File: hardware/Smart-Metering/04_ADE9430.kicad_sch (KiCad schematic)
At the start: 14 parts, among them U1 ADE9430ACPZ, Y1 24.576MHz

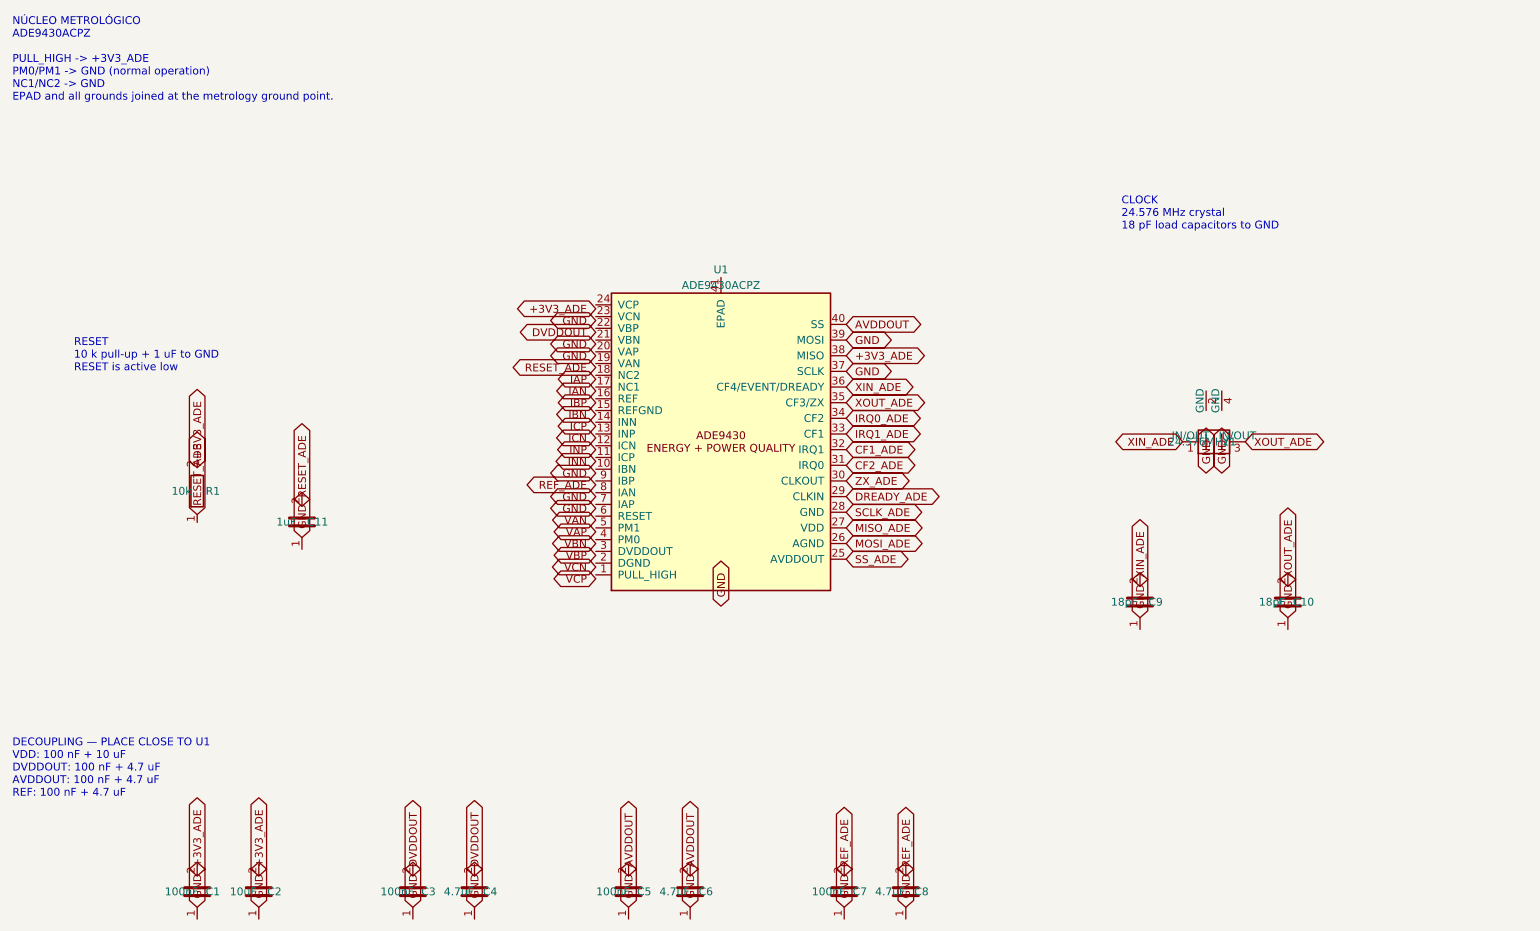
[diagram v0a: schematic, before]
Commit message: Corrige eixo Y dos símbolos próprios e ligações do ADE9430
Os símbolos de SmartMetering.kicad_sym foram escritos com o eixo Y
para baixo, mas o formato de biblioteca do KiCad usa Y para cima.
Com isso, na folha 04_ADE9430:

- os pinos 1-24 e o EPAD do U1 ficavam desconectados;
- os pinos 25-40 caíam em labels trocados (AVDDOUT em SS_ADE,
  VDD em MISO_ADE, SCLK/MOSI em GND etc.);
- os pinos GND do cristal Y1 ficavam desconectados;
- as pernas dos pinos verticais (R, C, cristal, EPAD) apontavam
  para fora do corpo do símbolo.

Correção: inverter o Y de pinos, propriedades e gráficos e orientar
os pinos verticais para o corpo, na biblioteca e na cópia embutida
na folha. Agora o pino 1 do ADE9430 fica no canto superior esquerdo
e todos os 69 pinos da folha caem nos nets previstos. O label GND
do EPAD passa a apontar para baixo.

Atualiza também a estrutura e o estado do projeto no README.

Co-Authored-By: Claude Opus 5.5 <noreply@anthropic.com>
Claude-Session: https://claude.ai/code/session_012B8cVkhtjf3eg98UdpNCpf
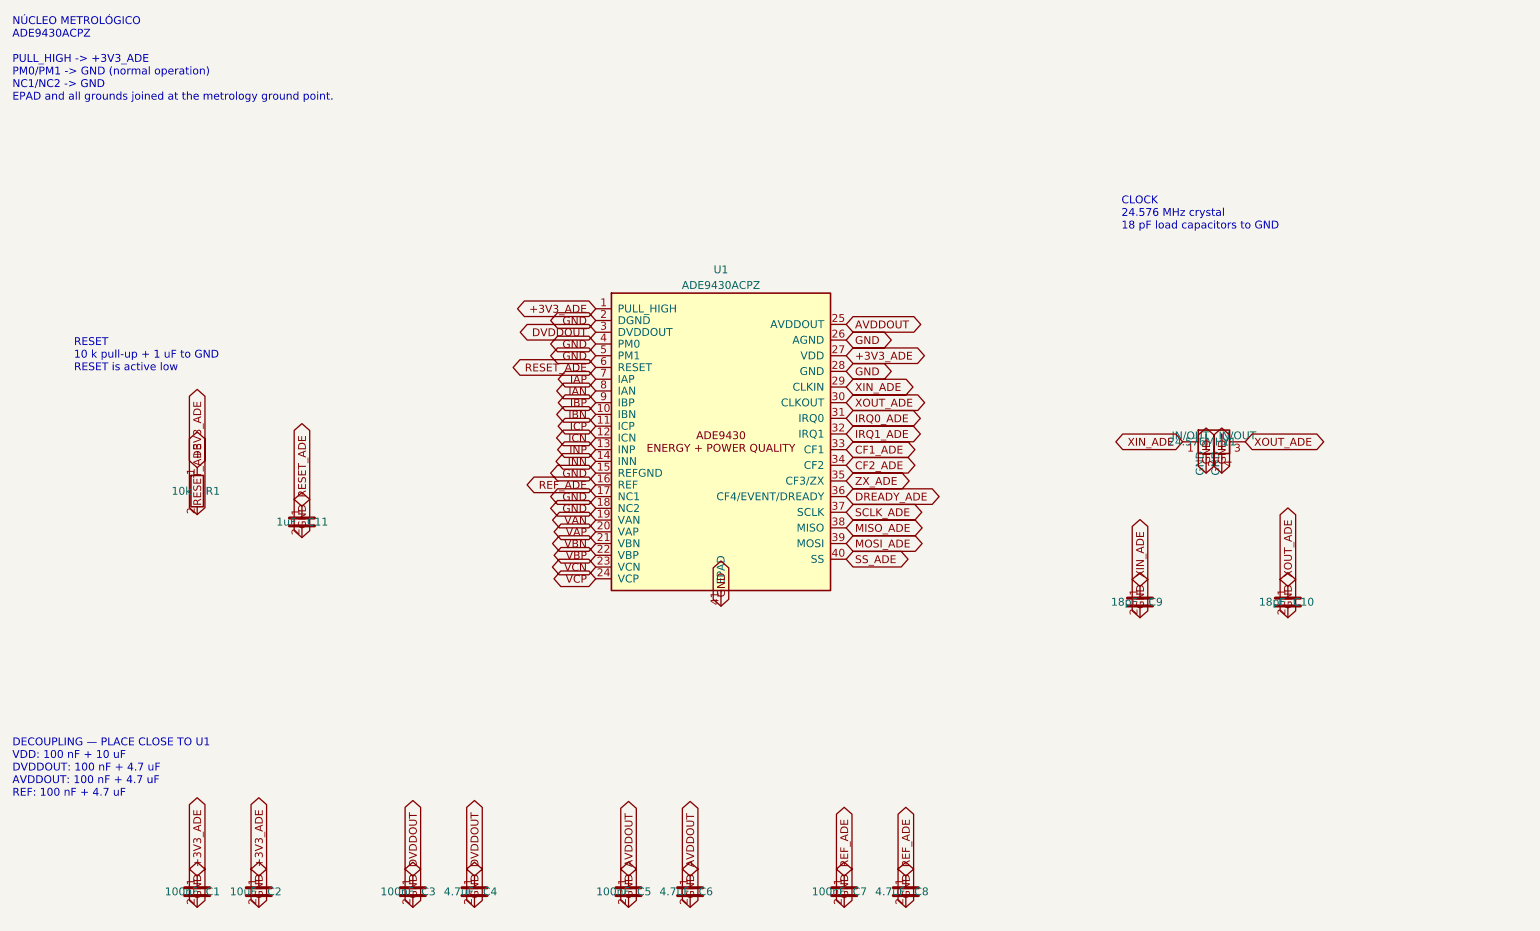
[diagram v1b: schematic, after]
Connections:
- net +3V3_ADE: now also C1.1, C2.1, R1.1, U1.1 (PULL_HIGH), U1.27 (VDD); no longer C1.2, C2.2, R1.2, U1.38 (MISO)
- net AVDDOUT: now also C5.1, C6.1, U1.25 (AVDDOUT); no longer C5.2, C6.2, U1.40 (SS)
- net CF1_ADE: now also U1.33 (CF1); no longer U1.32 (IRQ1)
- net CF2_ADE: now also U1.34 (CF2); no longer U1.31 (IRQ0)
- net DREADY_ADE: now also U1.36 (CF4/EVENT/DREADY); no longer U1.29 (CLKIN)
- net DVDDOUT: now also C3.1, C4.1, U1.3 (DVDDOUT); no longer C3.2, C4.2
- net GND: now also C1.2, C10.2, C11.2, C2.2, C3.2, C4.2, C5.2, C6.2, C7.2, C8.2, C9.2, U1.15 (REFGND), U1.17 (NC1), U1.18 (NC2), U1.2 (DGND), U1.26 (AGND), U1.28 (GND), U1.4 (PM0), U1.41 (EPAD), U1.5 (PM1), Y1.2 (GND), Y1.4 (GND); no longer C1.1, C10.1, C11.1, C2.1, C3.1, C4.1, C5.1, C6.1, C7.1, C8.1, C9.1, U1.37 (SCLK), U1.39 (MOSI)
- net IAN: now also U1.8 (IAN)
- net IAP: now also U1.7 (IAP)
- net IBN: now also U1.10 (IBN)
- net IBP: now also U1.9 (IBP)
- net ICN: now also U1.12 (ICN)
- net ICP: now also U1.11 (ICP)
- net INN: now also U1.14 (INN)
- net INP: now also U1.13 (INP)
- net IRQ0_ADE: now also U1.31 (IRQ0); no longer U1.34 (CF2)
- net IRQ1_ADE: now also U1.32 (IRQ1); no longer U1.33 (CF1)
- net MISO_ADE: now also U1.38 (MISO); no longer U1.27 (VDD)
- net MOSI_ADE: now also U1.39 (MOSI); no longer U1.26 (AGND)
- net REF_ADE: now also C7.1, C8.1, U1.16 (REF); no longer C7.2, C8.2
- net RESET_ADE: now also C11.1, R1.2, U1.6 (RESET); no longer C11.2, R1.1
- net SCLK_ADE: now also U1.37 (SCLK); no longer U1.28 (GND)
- net SS_ADE: now also U1.40 (SS); no longer U1.25 (AVDDOUT)
- net VAN: now also U1.19 (VAN)
- net VAP: now also U1.20 (VAP)
- net VBN: now also U1.21 (VBN)
- net VBP: now also U1.22 (VBP)
- net VCN: now also U1.23 (VCN)
- net VCP: now also U1.24 (VCP)
- net XIN_ADE: now also C9.1, U1.29 (CLKIN); no longer C9.2, U1.36 (CF4/EVENT/DREADY)
- net XOUT_ADE: now also C10.1, U1.30 (CLKOUT); no longer C10.2, U1.35 (CF3/ZX)
- net ZX_ADE: now also U1.35 (CF3/ZX); no longer U1.30 (CLKOUT)
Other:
- moved on the sheet: U1, Y1
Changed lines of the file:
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@@
 	(title_block
 		(title "ADE9430 - Metrology Core")
-		(date "2026-10-02")
-		(rev "0.2")
+		(date "2026-10-03")
+		(rev "0.3")
 		(company "Smart-Metering")
 		(comment 1 "ADE9430 core, decoupling, 24.576 MHz clock and reset network")
@@
 		(property "Intersheetrefs" "${INTERSHEET_REFS}" (at 160.32 111.05 0) (hide yes) (effects (font (size 1.27 1.27))))
 	)
-	(global_label "GND" (shape bidirectional) (at 140 118.67 90)
+	(global_label "GND" (shape bidirectional) (at 140 118.67 270)
 		(effects (font (size 1.27 1.27)) (justify left))
 		(property "Intersheetrefs" "${INTERSHEET_REFS}" (at 140 118.67 0) (hide yes) (effects (font (size 1.27 1.27))))

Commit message: Implementa folha de entrada de energia e numera referências por folha
01_Power_Input:
- modo padrão: LINE_A/B/C -> fusível -> diodo S1M em OU para o
  barramento HV, retorno no NEUTRAL via JP101; o instrumento segue
  alimentado com qualquer fase presente;
- modo auxiliar (J101, 100-240 VAC, com varistor): F104/D104/JP102,
  não montados por padrão; para rede 3 fios sem neutro;
- R101 fusível limita inrush, C101 4,7 uF/450 V no barramento;
- PS101 módulo AC/DC isolado 5 V / 2 A (ex.: IRM-10-5) gerando
  VIN_ACDC para a folha 09, referenciado a GND_SYS.

Referências renumeradas por folha para evitar colisões: folha 02 passa
a 2xx (R201 = ligação neutro/GND), folha 03 a 3xx e folha 04 a 4xx
(U401 = ADE9430).

Novos símbolos: D_Rect, CP_Vert, Jumper_2 e ACDC_Module.

Co-Authored-By: Claude Opus 5.5 <noreply@anthropic.com>
Claude-Session: https://claude.ai/code/session_012B8cVkhtjf3eg98UdpNCpf
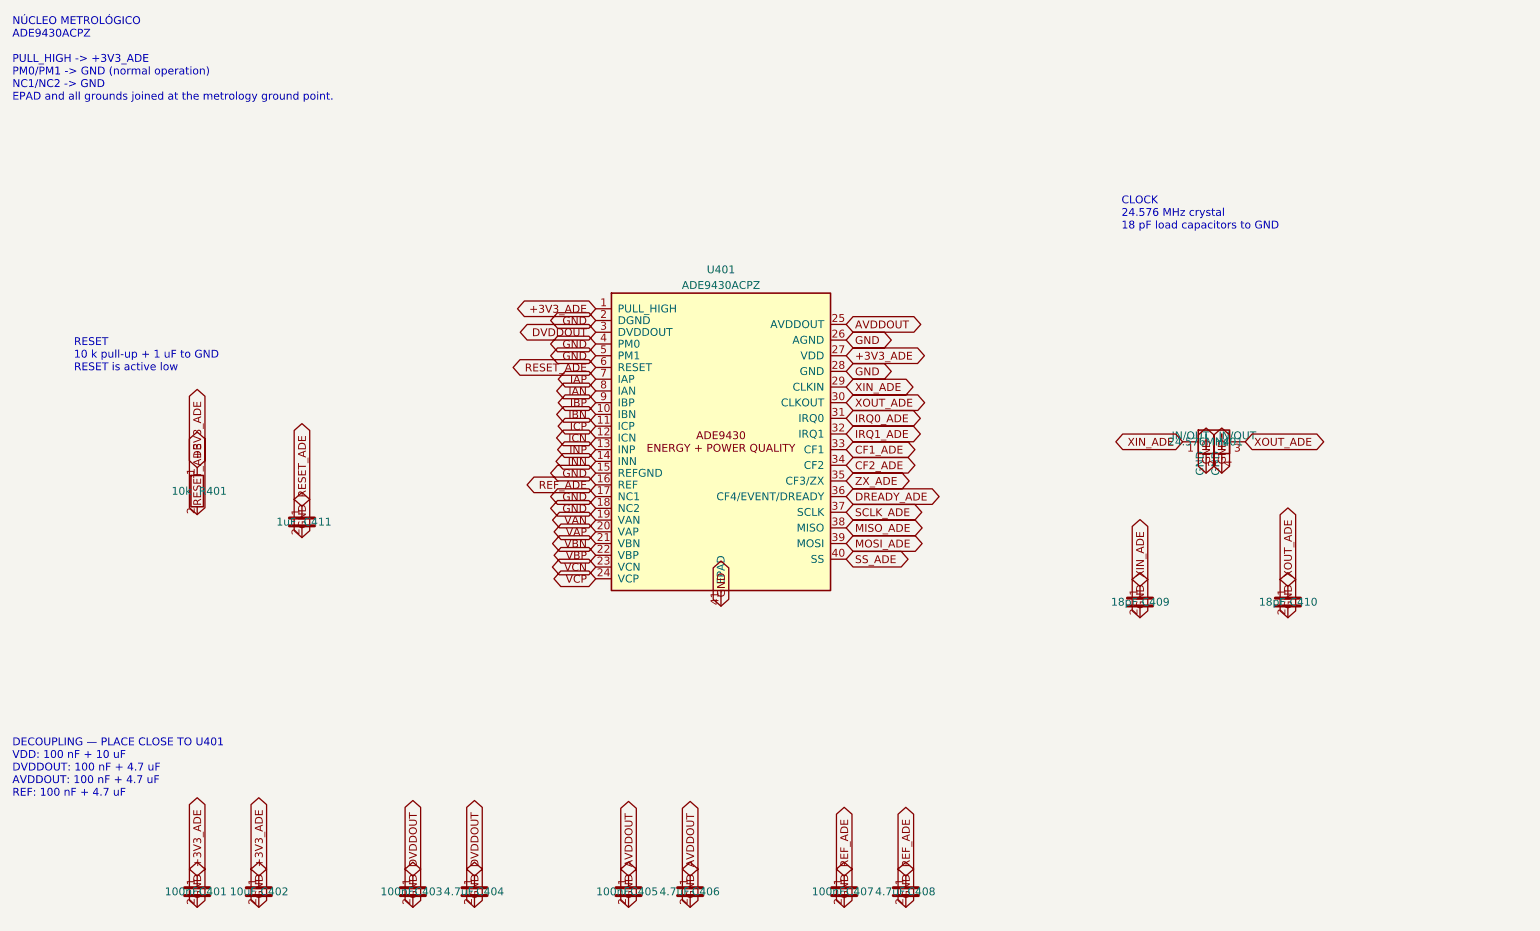
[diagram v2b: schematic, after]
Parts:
- renumbered C1 to C401, C2 to C402, C3 to C403, C4 to C404, C5 to C405, C6 to C406, C7 to C407, C8 to C408, C9 to C409, C10 to C410, C11 to C411, R1 to R401, U1 to U401, Y1 to Y401
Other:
- note added: "DECOUPLING — PLACE CLOSE TO U401 VDD: 100 nF + 10 uF DVDDOUT: 100 nF + 4.7 uF AVDDOUT: 100 nF + 4.7 uF REF: 100 nF + 4.7 uF"
- note removed: "DECOUPLING — PLACE CLOSE TO U1 VDD: 100 nF + 10 uF DVDDOUT: 100 nF + 4.7 uF AVDDOUT: 100 nF + 4.7 uF REF: 100 nF + 4.7 uF"

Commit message: Revisão completa do esquemático e correções
Verificação automática sobre o netlist global (215 componentes, 176 nets):
sem pinos soltos, sem nets de alimentação sem fonte, sem saídas em
conflito e isolação íntegra (terras só se encontram nas barreiras
PS101, PS601, U601, U602 e U801).

Correções:
- footprint do ADE9430 inexistente na biblioteca KiCad trocado por
  QFN-40 6x6 (tamanho do pad exposto a confirmar);
- MISO do ADE9430 como tri-state (barramento compartilhado com MCP3204);
- PS101 com símbolo e footprint oficiais do IRM-10-5 (o símbolo genérico
  tinha AC/L e AC/N trocados);
- PWR_FLAG em HV_DC, HV_RTN, VBAT_RTC, VDDA, GND_485 e VIN_CHG;
- footprints para fusíveis, varistores, indutores e chave de energia;
- polarização de fail-safe opcional no RS-485 (R807/R808, DNP);
- notas de layout (retorno do AC/DC) e de firmware (VBUS no PA9).

Relatório com revisão por folha, orçamento de potência e pendências em
docs/REVISAO_ESQUEMATICO.md.

Co-Authored-By: Claude Opus 5.5 <noreply@anthropic.com>
Claude-Session: https://claude.ai/code/session_012B8cVkhtjf3eg98UdpNCpf
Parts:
- U401: footprint Package_DFN_QFN:LFCSP-40-1EP_6x6mm_P0.5mm_EP4.5x4.5mm -> Package_DFN_QFN:QFN-40-1EP_6x6mm_P0.5mm_EP4.6x4.6mm
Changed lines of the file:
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@@
 		(property "Reference" "U401" (at 140 64.06 0) (effects (font (size 1.27 1.27))))
 		(property "Value" "ADE9430ACPZ" (at 140 66.6 0) (effects (font (size 1.27 1.27))))
-		(property "Footprint" "Package_DFN_QFN:LFCSP-40-1EP_6x6mm_P0.5mm_EP4.5x4.5mm" (at 140 92 0) (effects (font (size 1.27 1.27)) (hide yes)))
+		(property "Footprint" "Package_DFN_QFN:QFN-40-1EP_6x6mm_P0.5mm_EP4.6x4.6mm" (at 140 92 0) (effects (font (size 1.27 1.27)) (hide yes)))
 		(property "Datasheet" "https://www.analog.com/media/en/technical-documentation/data-sheets/ade9430.pdf" (at 140 92 0) (effects (font (size 1.27 1.27)) (hide yes)))
 		(property "Description" "High performance polyphase energy and Class S power quality monitoring IC" (at 140 92 0) (effects (font (size 1.27 1.27)) (hide yes)))
